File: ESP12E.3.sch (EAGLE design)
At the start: 25 parts, among them U1 SPX3819M5-L-3-3

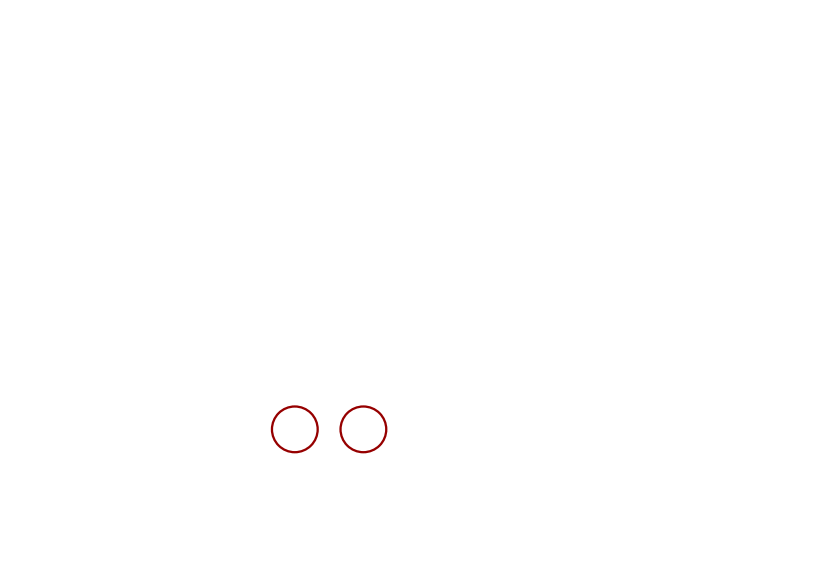
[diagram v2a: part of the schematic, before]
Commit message: //Increased board size and added M3 mounting holes
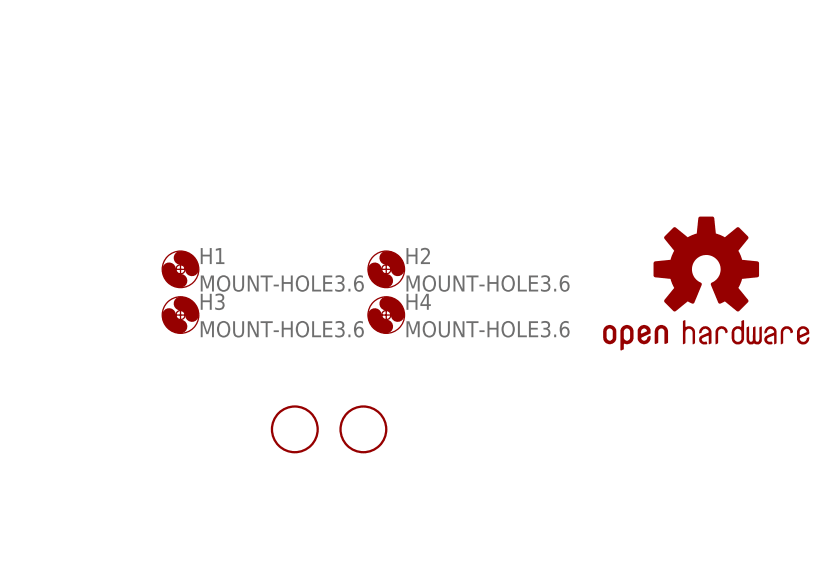
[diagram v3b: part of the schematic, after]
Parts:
- added H1, H2, H3, H4: MOUNT-HOLE3.6, holes:MOUNT-HOLE3.6
- added LOGO1: OSHW-LOGOMINI, SparkFun-Aesthetics:OSHW-LOGOMINI
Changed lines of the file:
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@@
 <?xml version="1.0" encoding="utf-8"?>
 <!DOCTYPE eagle SYSTEM "eagle.dtd">
-<eagle version="7.2.0">
+<eagle version="8.3.1">
 <drawing>
 <settings>
 <setting alwaysvectorfont="no"/>
+<setting keepoldvectorfont="yes"/>
 <setting verticaltext="up"/>
 </settings>
@@
 <part name="JP9" library="adafruit" deviceset="PINHD-1X3" device=""/>
 <part name="JP11" library="adafruit" deviceset="PINHD-1X3" device=""/>
+<part name="H1" library="holes" library_urn="urn:adsk.eagle:library:237" deviceset="MOUNT-HOLE" device="3.6" package3d_urn="urn:adsk.eagle:package:14272/1"/>
+<part name="H2" library="holes" library_urn="urn:adsk.eagle:library:237" deviceset="MOUNT-HOLE" device="3.6" package3d_urn="urn:adsk.eagle:package:14272/1"/>
+<part name="H3" library="holes" library_urn="urn:adsk.eagle:library:237" deviceset="MOUNT-HOLE" device="3.6" package3d_urn="urn:adsk.eagle:package:14272/1"/>
+<part name="H4" library="holes" library_urn="urn:adsk.eagle:library:237" deviceset="MOUNT-HOLE" device="3.6" package3d_urn="urn:adsk.eagle:package:14272/1"/>
+<part name="LOGO1" library="SparkFun-Aesthetics" deviceset="OSHW-LOGO" device="MINI"/>
 </parts>
 <sheets>
@@
 <instance part="JP9" gate="A" x="106.68" y="124.46"/>
 <instance part="JP11" gate="A" x="119.38" y="124.46"/>
+<instance part="H1" gate="G$1" x="330.2" y="45.72"/>
+<instance part="H2" gate="G$1" x="353.06" y="45.72"/>
+<instance part="H3" gate="G$1" x="330.2" y="40.64"/>
+<instance part="H4" gate="G$1" x="353.06" y="40.64"/>
+<instance part="LOGO1" gate="G$1" x="388.62" y="45.72"/>
 </instances>
 <busses>
@@
 which will not be processed correctly with this version.
 </note>
+<note version="8.2" severity="warning">
+Since Version 8.2, EAGLE supports online libraries. The ids
+of those online libraries will not be understood (or retained)
+with this version.
+</note>
+<note version="8.3" severity="warning">
+Since Version 8.3, EAGLE supports URNs for individual library
+assets (packages, symbols, and devices). The URNs of those assets
+will not be understood (or retained) with this version.
+</note>
+<note version="8.3" severity="warning">
+Since Version 8.3, EAGLE supports the association of 3D packages
+with devices in libraries, schematics, and board files. Those 3D
+packages will not be understood (or retained) with this version.
+</note>
 </compatibility>
